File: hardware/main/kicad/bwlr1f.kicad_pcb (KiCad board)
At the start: 4 copper layers, 61.2 x 26.1 mm, 61 parts, among them J1 Conn_01x02, U1 RAK3172-SIP, U2 NBM7100ABQX, U3 ZD24C08A, U4 BME688, U5 RV-3028-C7

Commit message: Update Programmer
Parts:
- moved C21 0.31 mm to (143.8, 120.2)
- moved C12 0.15 mm to (143.8, 103.8)
- moved C13 0.15 mm to (145.0, 103.8)
- moved L3 0.15 mm to (142.8, 103.8)
- moved L4 0.15 mm to (146.0, 103.8)
- moved C11 0.13 mm to (143.1, 100.3)
- moved C15 0.10 mm to (136.9, 114.3)
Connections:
- U1 pad 14: unconnected-(U1-PB3-Pad14) -> /RTC_WKUP
- U1 pad 5: /RTC_WKUP -> unconnected-(U1-PC13-Pad5)
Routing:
- net /RTC_WKUP: track 8.42 -> 15.2 mm
- net /SCL: track 62.4 -> 59.1 mm, vias 5 -> 6
- net +3V0: track 56.1 -> 53.1 mm, vias 12 -> 11
- net GND: track 27.2 -> 29.3 mm, vias 108 -> 103
- net /RDY: track 4.51 -> 6.55 mm

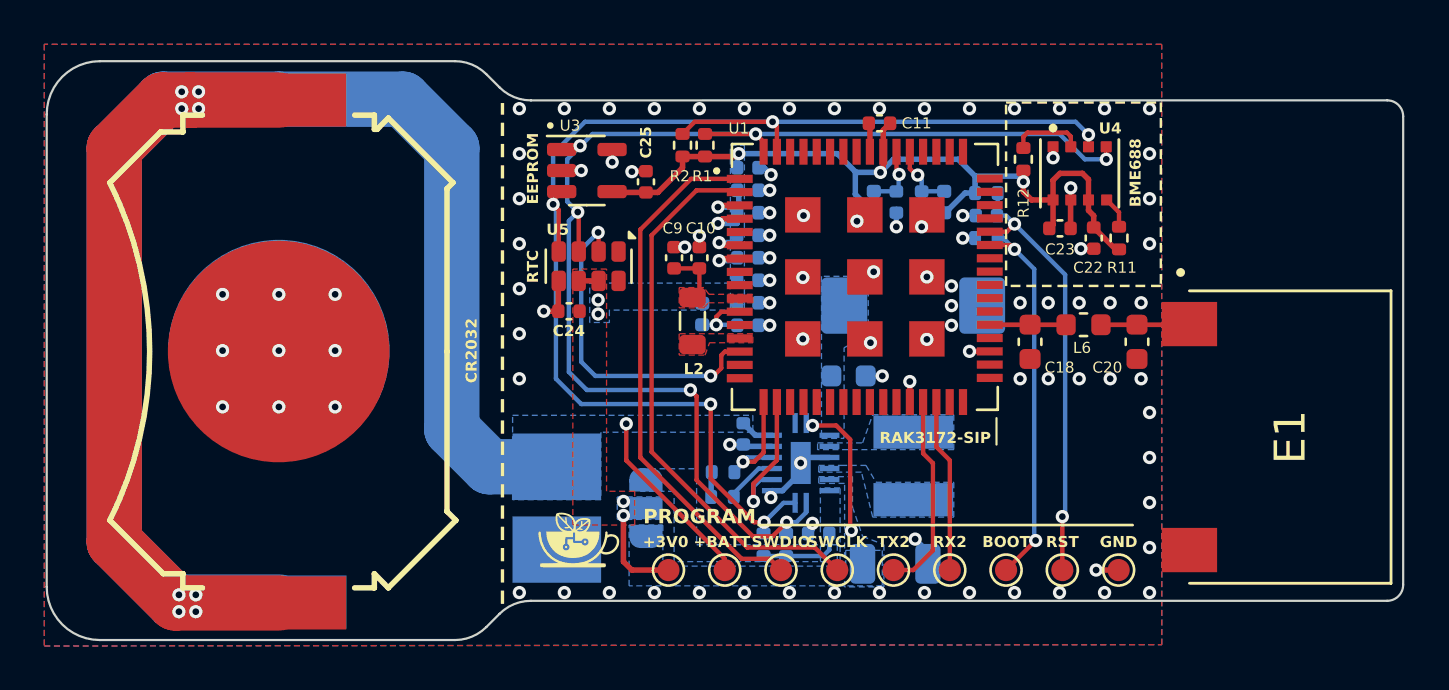
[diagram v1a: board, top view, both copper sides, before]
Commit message: Added ESD to main board
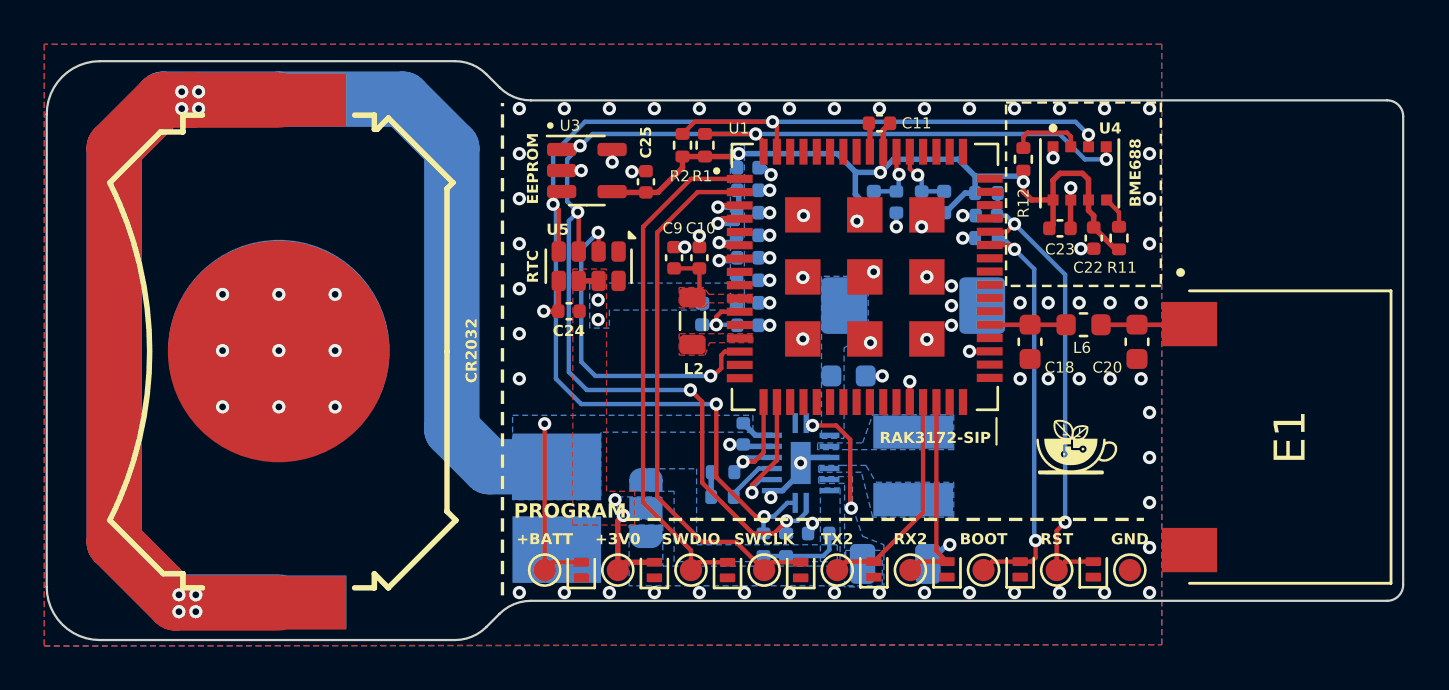
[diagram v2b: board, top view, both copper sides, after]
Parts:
- added D1: ESD5651N, Diode_SMD:D_SOD-882, F.Cu at (149.4, 120.4)
- added D2: ESD5651N, Diode_SMD:D_SOD-882, F.Cu at (152.7, 120.4)
- added D3: ESD5651N, Diode_SMD:D_SOD-882, F.Cu at (136.2, 120.5)
- added D4: ESD5651N, Diode_SMD:D_SOD-882, F.Cu at (139.5, 120.5)
- added D5: ESD5651N, Diode_SMD:D_SOD-882, F.Cu at (142.8, 120.4)
- added D6: ESD5651N, Diode_SMD:D_SOD-882, F.Cu at (146.1, 120.4)
- added D7: ESD5651N, Diode_SMD:D_SOD-882, F.Cu at (129.6, 120.5)
- added D8: ESD5651N, Diode_SMD:D_SOD-882, F.Cu at (132.9, 120.5)
- moved G*** 22.9 mm to (152.0, 114.9)
- moved TP2 8.13 mm to (127.9, 120.5)
- moved TP6 4.06 mm to (134.6, 120.5)
- moved TP5 3.30 mm to (137.9, 120.5)
- moved TP4 2.54 mm to (141.2, 120.5)
- moved TP1 2.29 mm to (131.3, 120.5)
- moved TP3 1.78 mm to (144.5, 120.5)
- moved TP8 1.02 mm to (147.8, 120.5)
- moved TP9 0.51 mm to (154.4, 120.5)
- moved TP7 0.25 mm to (151.1, 120.5)
- renumbered TP8 to TP1, TP10 to TP2, TP1 to TP3, TP2 to TP4, TP3 to TP5, TP4 to TP6, TP5 to TP7, TP6 to TP8
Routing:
- net /RST: track 19.9 -> 21.8 mm
- net /BOOT: track 17.6 -> 19.1 mm
- net /RX2: track 7.83 -> 9.21 mm
- net GND: track 29.3 -> 28.2 mm, vias 103 -> 102
- net Net-(JP1-B): track 6.43 -> 5.41 mm
- net /TX2: track 9.02 -> 9.93 mm
- net /SWCLK: track 25.2 -> 24.4 mm
- net /RDY: track 6.55 -> 5.81 mm
- net /SWDIO: track 24.2 -> 23.4 mm

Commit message: Update for Programmer
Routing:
- net GND: track 28.2 -> 32.4 mm
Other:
- board text added: "Dimension @User.2"
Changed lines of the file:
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@@
 		)
 	)
+	(gr_text "Dimension @User.2"
+		(at 105.469999 126.303 0)
+		(layer "User.2")
+		(effects
+			(font
+				(size 1 1)
+				(thickness 0.15)
+			)
+			(justify left bottom)
+		)
+	)
 	(dimension
 		(type aligned)
 		(layer "User.2")
 		(pts
-			(xy 107.869999 97.489999) (xy 107.869999 123.62)
+			(xy 165.981847 99.257376) (xy 165.981847 121.84911)
 		)
-		(height -63.132)
-		(gr_text "26,1300 mm"
-			(at 169.851999 110.555 90)
+		(height -4.004152)
+		(gr_text "22,5917 mm"
+			(at 171.001999 110.555 90)
 			(layer "User.2")
 			(effects
@@
 			(thickness 0.15)
 			(arrow_length 1.27)
-			(text_position_mode 0)
+			(text_position_mode 2)
 			(extension_height 0.58642)
 			(extension_offset 0.5) keep_text_aligned)
@@
 			(xy 105.469999 110.555) (xy 166.702471 110.553)
 		)
-		(height -23.799694)
+		(height -16.394027)
 		(gr_text "61,2325 mm"
-			(at 136.08542 85.604306 0.001871418142)
+			(at 136.085662 93.009973 0.001871418142)
+			(layer "User.2")
+			(effects
+				(font
+					(size 1 1)
+					(thickness 0.15)
+				)
+			)
+		)
+		(format
+			(prefix "")
+			(suffix "")
+			(units 3)
+			(units_format 1)
+			(precision 4)
+		)
+		(style
+			(thickness 0.15)
+			(arrow_length 1.27)
+			(text_position_mode 0)
+			(extension_height 0.58642)
+			(extension_offset 0.5) keep_text_aligned)
+	)
+	(dimension
+		(type aligned)
+		(layer "User.2")
+		(pts
+			(xy 107.869999 97.489999) (xy 107.869999 123.62)
+		)
+		(height 5.447999)
+		(gr_text "26,1300 mm"
+			(at 101.272 110.555 90)
 			(layer "User.2")
 			(effects
@@
 	)
 	(segment
+		(start 156.763999 119.558)
+		(end 155.507999 118.302)
+		(width 0.25)
+		(layer "F.Cu")
+		(net 1)
+	)
+	(segment
 		(start 151.688999 103.763)
 		(end 151.697999 103.754)
@@
 	)
 	(segment
+		(start 156.791999 119.558)
+		(end 155.507999 120.842)
+		(width 0.25)
+		(layer "F.Cu")
+		(net 1)
+	)
+	(segment
+		(start 157.053999 119.558)
+		(end 156.763999 119.558)
+		(width 0.25)
+		(layer "F.Cu")
+		(net 1)
+	)
+	(segment
 		(start 134.270999 105.884)
 		(end 133.790999 105.884)
@@
 	)
 	(segment
+		(start 157.053999 119.558)
+		(end 156.791999 119.558)
+		(width 0.25)
+		(layer "F.Cu")
+		(net 1)
+	)
+	(segment
 		(start 147.125999 110.588)
 		(end 148.041847 110.588)
@@
 		(layers "F.Cu" "In1.Cu" "In2.Cu" "B.Cu")
 		(hatch edge 0.5)
-		(connect_pads yes
+		(connect_pads
 			(clearance 0.2)
 		)
@@
 		(filled_areas_thickness no)
 		(fill yes
-			(thermal_gap 0.5)
-			(thermal_bridge_width 0.5)
+			(thermal_gap 0.2)
+			(thermal_bridge_width 0.2)
 		)
 		(polygon

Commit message: Finish Production File for Main Board
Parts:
- TP1: value 3V0 -> 90055-AS
- TP2: value BATT+ -> 90055-AS
- TP3: value RX2 -> 90055-AS
- TP4: value TX2 -> 90055-AS
- TP5: value SWCLK -> 90055-AS
- TP6: value SWDIO -> 90055-AS
- TP7: value RST -> 90055-AS
- TP8: value BOOT -> 90055-AS
- TP9: value GND -> 90055-AS

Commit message: Finish Production File for Programmer Board
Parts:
- TP1, TP2, TP3, TP4, TP5, TP6, TP7, TP8, TP9: value 90055-AS -> ProgPin
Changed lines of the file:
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@@
 			)
 		)
-		(property "Value" "90055-AS"
+		(property "Value" "ProgPin"
 			(at 0 -2.286 0)
 			(layer "F.Fab")
@@
 			)
 		)
-		(property "Value" "90055-AS"
+		(property "Value" "ProgPin"
 			(at 0 2.286 0)
 			(layer "F.Fab")
@@
 			)
 		)
-		(property "Value" "90055-AS"
+		(property "Value" "ProgPin"
 			(at 0 -2.286 0)
 			(layer "F.Fab")
@@
 			)
 		)
-		(property "Value" "90055-AS"
+		(property "Value" "ProgPin"
 			(at 1.514153 0.0618 0)
 			(layer "F.Fab")
@@
 			)
 		)
-		(property "Value" "90055-AS"
+		(property "Value" "ProgPin"
 			(at 0 -2.286 180)
 			(layer "F.Fab")
@@
 			)
 		)
-		(property "Value" "90055-AS"
+		(property "Value" "ProgPin"
 			(at -2.286 0 180)
 			(layer "F.Fab")
@@
 			)
 		)
-		(property "Value" "90055-AS"
+		(property "Value" "ProgPin"
 			(at 0 -2.286 0)
 			(layer "F.Fab")
@@
 			)
 		)
-		(property "Value" "90055-AS"
+		(property "Value" "ProgPin"
 			(at 0 -2.286 0)
 			(layer "F.Fab")
@@
 			)
 		)
-		(property "Value" "90055-AS"
+		(property "Value" "ProgPin"
 			(at 0 -2.301553 0)
 			(layer "F.Fab")
